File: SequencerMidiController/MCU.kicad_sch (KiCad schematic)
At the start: 7 parts, among them U33 STM32G0B1_KxTxN_LQFP32

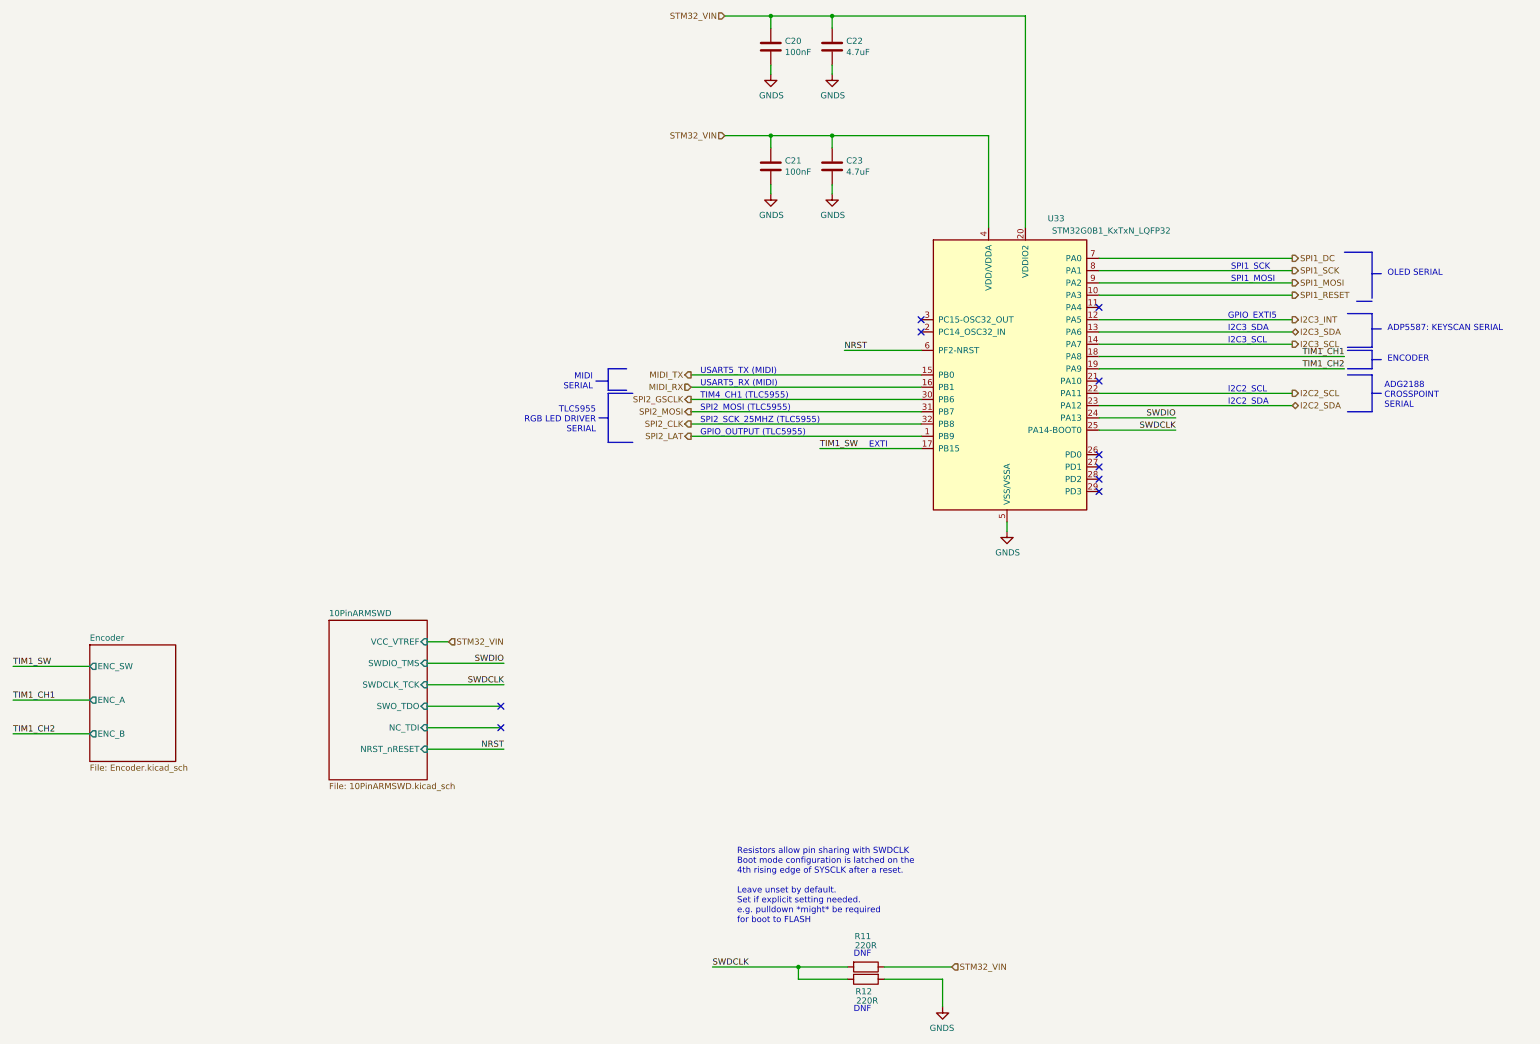
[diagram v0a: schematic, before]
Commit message: Checked microSD card connector pins and added board layout connector footprint
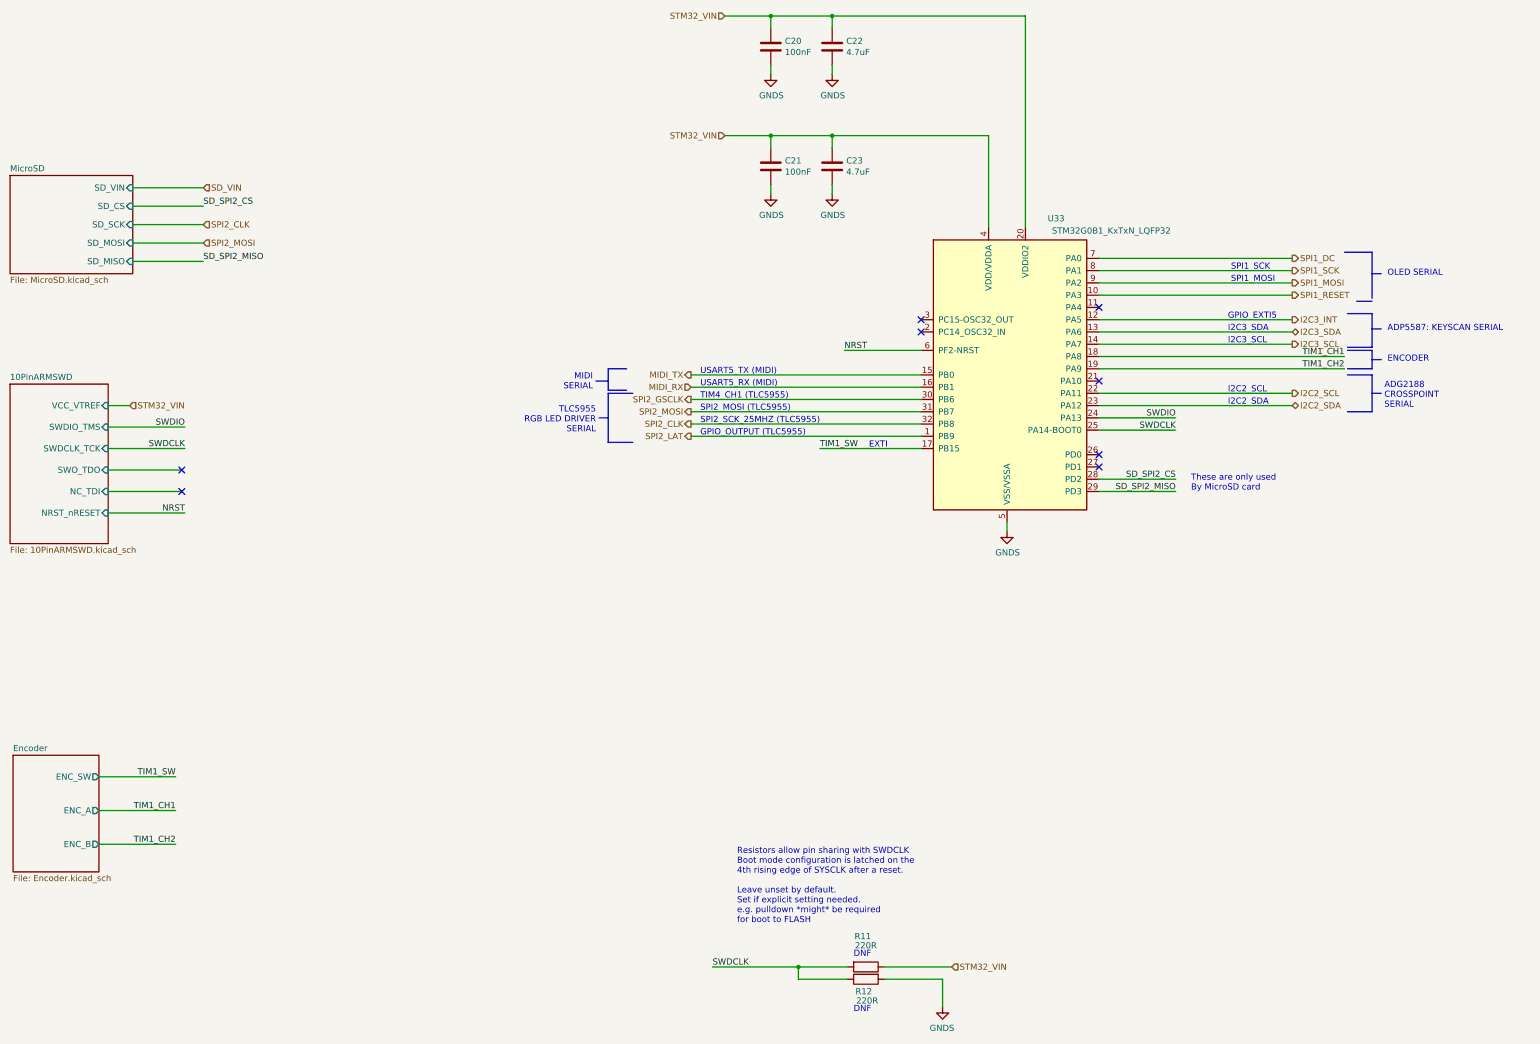
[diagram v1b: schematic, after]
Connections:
- net SD_SPI2_CS: now reaches U33.28 (PD2)
- net SD_SPI2_MISO: now reaches U33.29 (PD3)
- no-connect marks 10 -> 8
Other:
- added sheet MicroSD (MicroSD.kicad_sch)
- note added: "These are only used By MicroSD card"
